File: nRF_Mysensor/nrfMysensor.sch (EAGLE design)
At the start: 16 parts, among them IC1 3.3V

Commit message: Added  Nrf24 Arduino Mysensor node
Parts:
- removed IC1: 3.3V, 1AA_Stofer:MCP1703ASOT223
- removed SV1: (no value), con-lstb:MA07-2
- added 5VUART, JP1: (no value), SparkFun-Connectors:M06SIP
- added ADC6, D4, D5, D6, INT0, INT1: SOLDER_POINTA, 1AA_Stofer:SOLDER_POINTA
- added C10, C4, C5, C6: 0.1uF, SparkFun:CAP0805
- added C19: 10uF, SparkFun:CAP_POL7343
- added C7: 8uf/6v, rcl:CPOL-USSMCB
- added J1: 12V input, dp_devices:CON_HEADER_1X02-PTH
- added Q1: 16MHz resonator, SparkFun:RESONATORSMD
- added R13: 10K, SparkFun:RESISTOR0603
- added R5: 1K, SparkFun:RESISTOR0603
- added SJ1: SOLDERJUMPERNO, SparkFun-Passives:SOLDERJUMPERNO
- added U1: ATMEGA328P-AU(R), SparkFun:ATMEGA168
- added VR1: MCP1703T-3302E/DBCT-ND, 1AA_Stofer:MCP1703ASOT223
- added VR2: MCP1703A-5002E/DB-ND, 1AA_Stofer:MCP1703ASOT223
- C1: value 22uf/6v Non electroytic -> 8uf/6v
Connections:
- removed net A4: SV1.5
- removed net A5: SV1.3
- removed net A6: SV1.6
- removed net A7: C3.1, R2.1, R3.2, SV1.4
- removed net CE: SV1.13, SV2.4
- removed net CSN: SV1.1, SV2.3
- removed net D11: C3.2, R3.1, SV1.2, U$1.P$1
- removed net MISO: SV1.8, SV2.8
- removed net MOSI: SV1.9, SV2.5
- removed net RES: SV1.12
- removed net SCK: SV1.10, SV2.6
- removed net VCC_5V: IC1.V_IN, SV1.7
- new net 12V_INPUT: C19.+, J1.2, VR2.V_IN
- new net 5V: C10.1, C4.2, C7.+, R13.2, SJ1.1, U1.AVCC, U1.VCC@1, U1.VCC@2, VR1.V_IN, VR2.V_OUT
- new net A0_PC0: JP1.1, U1.PC0(ADC0)
- new net A1_PC1: JP1.2, U1.PC1(ADC1)
- new net A2_PC2: JP1.3, U1.PC2(ADC2)
- new net A3_PC3: JP1.4, U1.PC3(ADC3)
- new net A4_PC4_SDA: JP1.5, U1.PC4(ADC4/SDA)
- new net A5_PC5_SCL: JP1.6, U1.PC5(ADC5/SCL)
- new net ADC6: ADC6.P$1, U1.ADC6
- new net ADC7: C3.1, R2.1, R3.2, U1.ADC7
- new net AREF: C5.2, U1.AREF
- new net D10_PB2: SV2.3, U1.PB2(SS/OC1B)
- new net D11_PB3_MOSI: SV2.5, U1.PB3(MOSI/OC2)
- new net D12_PB4_MISO: SV2.8, U1.PB4(MISO)
- new net D13_PB5_SCK: SV2.6, U1.PB5(SCK)
- new net D4_PD4: D4.P$1, U1.PD4(XCK/T0)
- new net D5_PD5: D5.P$1, U1.PD5(T1)
- new net D6_PD6: D6.P$1, U1.PD6(AIN0)
- new net D7_PD7: C3.2, R3.1, U$1.P$1, U1.PD7(AIN1)
- new net D9: SV2.4, U1.PB1(OC1A)
- new net INT0: INT0.P$1, U1.PD2(INT0)
- new net INT1: INT1.P$1, U1.PD3(INT1)
- new net N$3: 5VUART.3, R5.2
- new net N$4: 5VUART.4, SJ1.2
- new net N$5: Q1.1, U1.PB7(XTAL2/TOSC2)
- new net N$6: 5VUART.1, C6.2
- new net N$9: Q1.3, U1.PB6(XTAL1/TOSC1)
- new net RESET: C6.1, R13.1, U1.PC6(/RESET)
- new net RXI: R5.1, U1.PD0(RXD)
- new net TXO: 5VUART.2, U1.PD1(TXD)
- net D8: now also U1.PB0(ICP); no longer SV1.14
- net GND: now also 5VUART.5, 5VUART.6, C10.2, C19.-, C4.1, C5.1, C7.-, J1.1, Q1.2, U1.AGND, U1.GND@1, U1.GND@2, VR1.GND, VR1.TAB, VR2.GND, VR2.TAB; no longer IC1.GND, SV1.11
- net VCC3_3: now also VR1.V_OUT; no longer IC1.V_OUT
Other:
- note added: "/CS"
- note added: "Battery operation: Remove VR1 and VR2, open SJ1 and jumper VR1."
- note added: "Battery operation: program Fuses for 8mhz internal clk, 1.8V brownout"
- note added: "Battery: MAX 3.6V"
- note added: "C1 Non electrolyte"
- note added: "DTR"
- note added: "FTDI UART / Arduino Programmer"
- note added: "Jumper for 5V operation from UART only if VR1 is present"
- note added: "RXI"
- note added: "TXO"
- note added: "VCC5V"
- note added: "ce"
- note added: "gnd"
- note added: "miso"
- note added: "mosi"
- note added: "pin1 indication on NRF bd is incorrect"
- note added: "sck"
- note added: "vcc33"
- note removed: "Cut connection to D11 on the Arduino pcb and wire SV1,Pin2 to D7 via high wire."
- note removed: "D10"
- note removed: "D7 via wire"
- note removed: "D9"
- note removed: "Interface board between Arduino Pro mini and nRF24L"
- note removed: "PCBs can be ordered directly at https://oshpark.com/shared_projects/PWLCreWN for $1 each."
- note removed: "Power Arduino Pro mini with 3.3V serial adapter for programming."
- note removed: "Pro Mini with 14 pin dual row header (SV1)"
- note removed: "Remove 5V regulator on Arduino Pro Mini."
- note removed: "SV1 Pin2 is connected to D11 (aka MOSI) on the Aurduino pcb."
- note removed: "Voltage divider for battery test"
- moved on the sheet: BAT+, BAT-, C1, C2, C3, L1, L2, R1, R2, R3, R4, SP1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

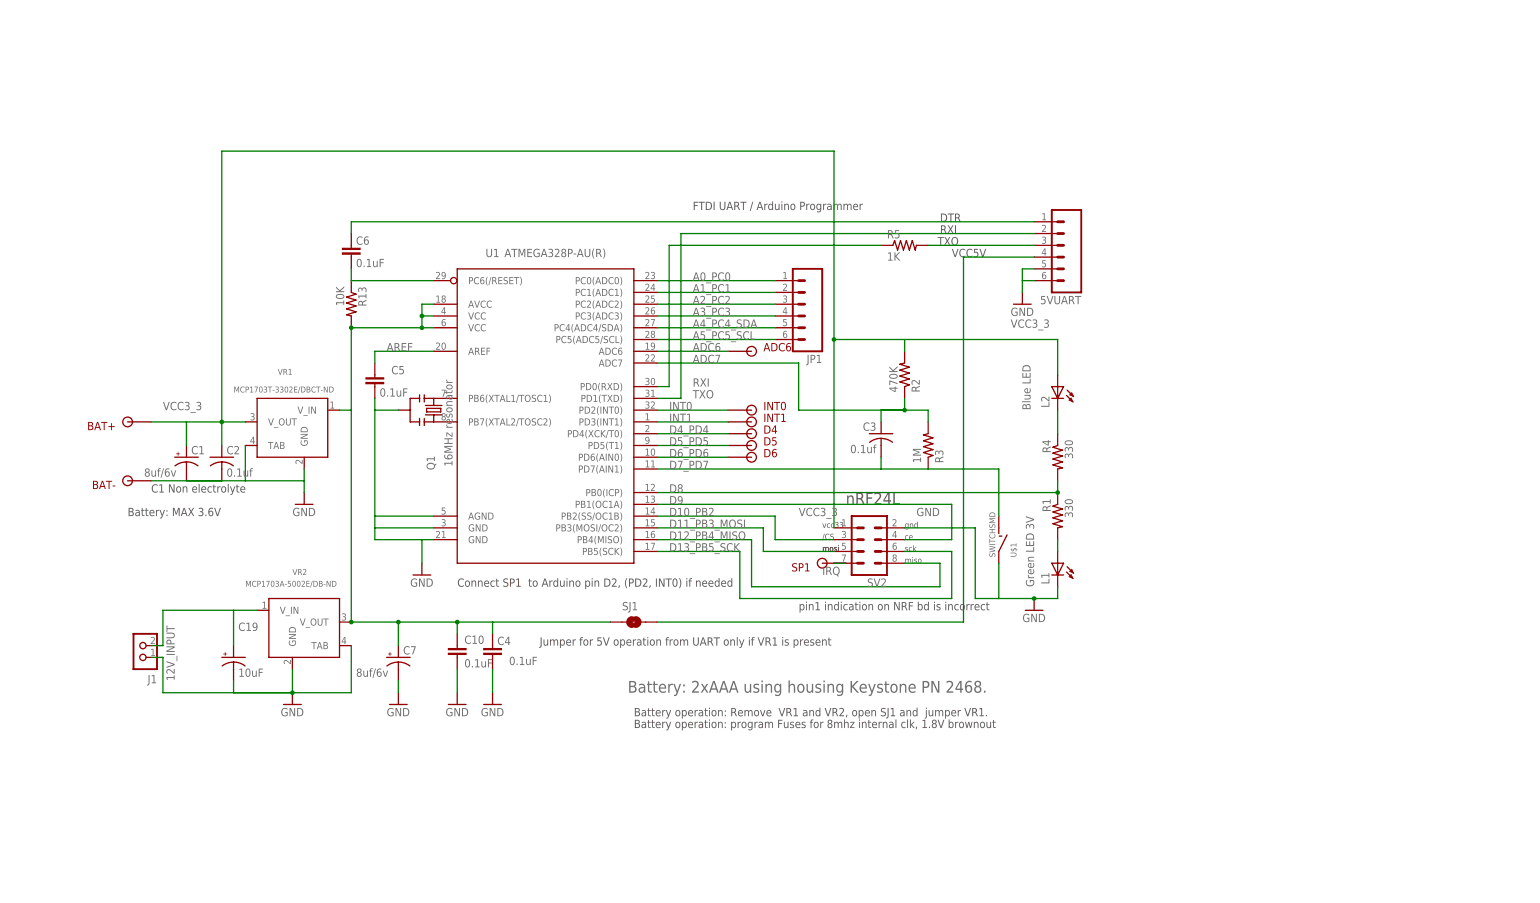
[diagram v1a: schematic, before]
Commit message: nRF_MySensor board: Added resistor position for external pull up on PC0. Added spare GND and VCC solder points. Fixed R2/R3 values swapped Added more detailed build option instructions.
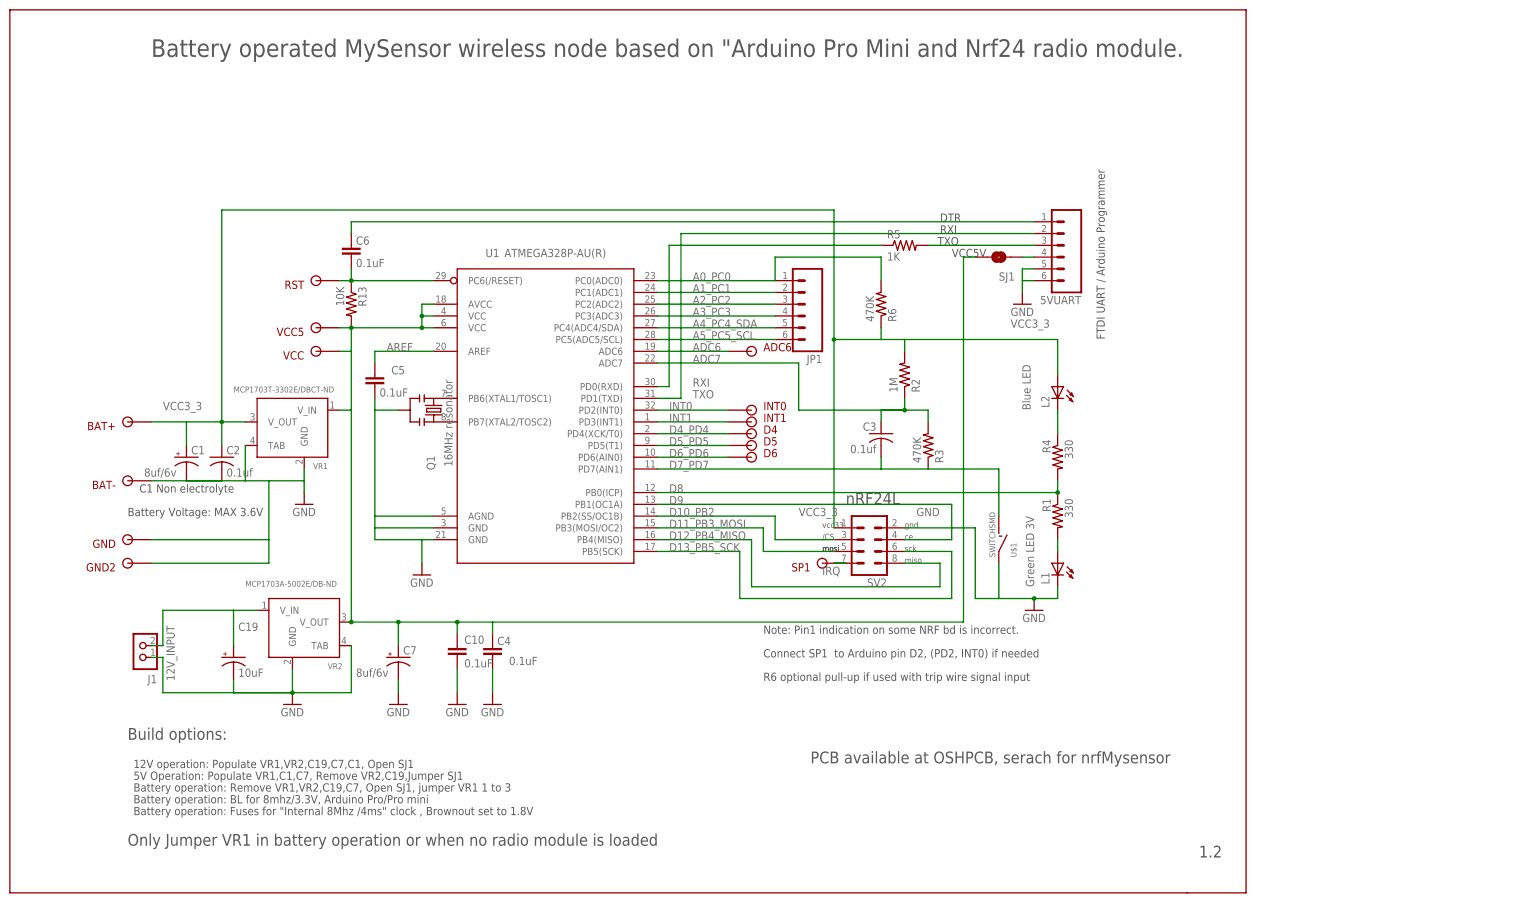
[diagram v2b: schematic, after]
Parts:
- added GND, GND2, RST, VCC, VCC5: SOLDER_POINTA, 1AA_Stofer:SOLDER_POINTA
- added R6: 470K, rcl:R-US_R0603
- R2: value 470K -> 1M
- R3: value 1M -> 470K
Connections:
- net 5V: now also VCC.P$1, VCC5.P$1
- net A0_PC0: now also R6.2
- net GND: now also GND.P$1, GND2.P$1
- net RESET: now also RST.P$1
- net VCC3_3: now also R6.1
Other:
- note added: "1.2"
- note added: "12V operation: Populate VR1,VR2,C19,C7,C1, Open SJ1"
- note added: "5V Operation: Populate VR1,C1,C7, Remove VR2,C19,Jumper SJ1"
- note added: "Battery Voltage: MAX 3.6V"
- note added: "Battery operated MySensor wireless node based on "Arduino Pro Mini and Nrf24 radio module."
- note added: "Battery operation: BL for 8mhz/3.3V, Arduino Pro/Pro mini"
- note added: "Battery operation: Fuses for "Internal 8Mhz /4ms" clock , Brownout set to 1.8V"
- note added: "Battery operation: Remove VR1,VR2,C19,C7, Open SJ1, jumper VR1 1 to 3"
- note added: "Build options:"
- note added: "Note: Pin1 indication on some NRF bd is incorrect."
- note added: "Only Jumper VR1 in battery operation or when no radio module is loaded"
- note added: "PCB available at OSHPCB, serach for nrfMysensor"
- note added: "R6 optional pull-up if used with trip wire signal input"
- note removed: "Battery operation: Remove VR1 and VR2, open SJ1 and jumper VR1."
- note removed: "Battery operation: program Fuses for 8mhz internal clk, 1.8V brownout"
- note removed: "Battery: 2xAAA using housing Keystone PN 2468."
- note removed: "Battery: MAX 3.6V"
- note removed: "Jumper for 5V operation from UART only if VR1 is present"
- note removed: "pin1 indication on NRF bd is incorrect"
- moved on the sheet: SJ1
